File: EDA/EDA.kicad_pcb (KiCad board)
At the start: 2 copper layers, 75.4 x 53.8 mm, 46 parts, among them J2 Screw_Terminal_01x02, M1 Motor_Servo, U1 PMCF8316A1VRGFR, U2 LM2596S-5, U3 LM2678S-5

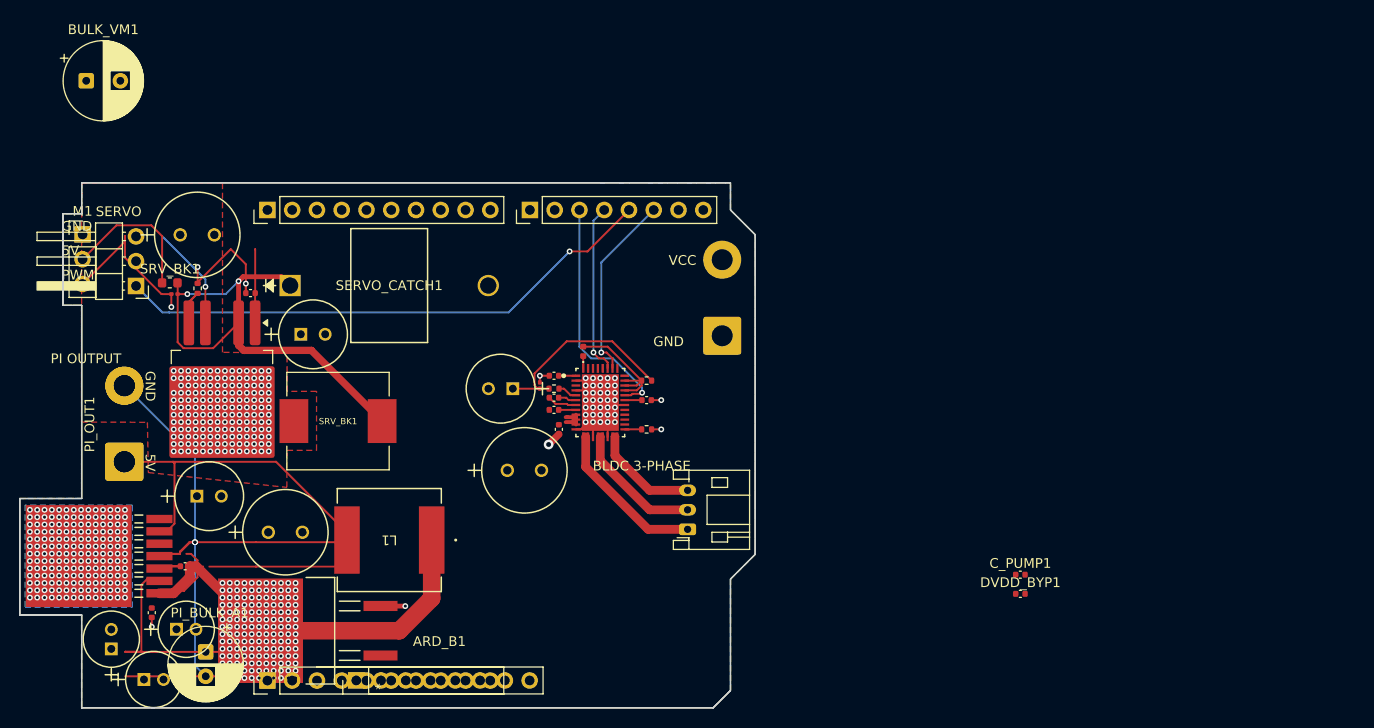
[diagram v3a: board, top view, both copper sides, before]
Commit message: Add initial EDA project files and configuration
- Created EDA.step file for project steps.
- Added autosave configuration for EDA.kicad_prl with board settings, visibility options, and net inspector panel configurations.
- Introduced lock files for PCB and schematic with hostname and username information.
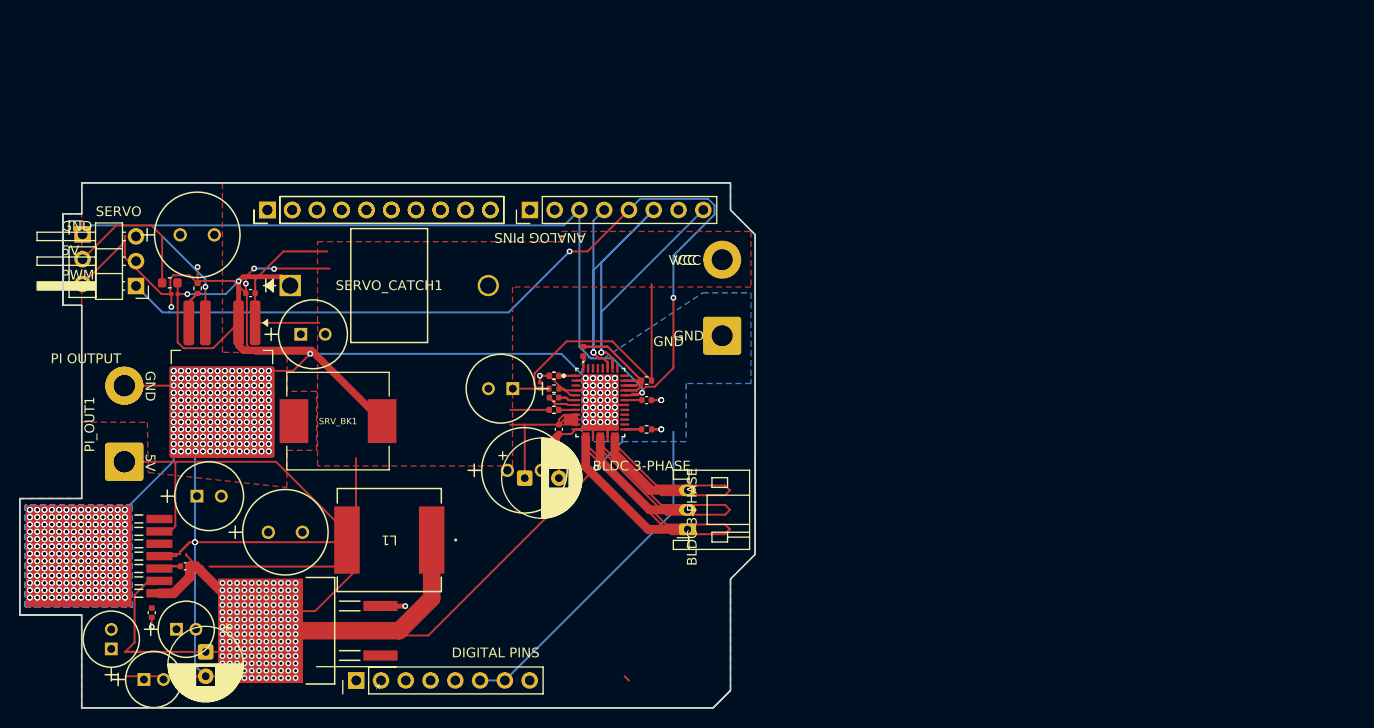
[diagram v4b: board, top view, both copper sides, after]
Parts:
- removed the ARD_B1 at (124.9, 73.8)
- removed the ARD_B1 at (124.9, 122.0)
- removed the C_PUMP1 at (154.2, 94.2)
- removed the C_PUMP1 at (202.1, 111.2)
- removed the DVDD_BYP1 at (154.2, 90.8)
- removed the DVDD_BYP1 at (202.1, 113.1)
- removed the PI_OUT1 at (110.2, 99.6) (x2)
- added ARD_B1 (x2): Conn_01x10_Pin, Connector_PinHeader_2.54mm:PinHeader_1x10_P2.54mm_Vertical, F.Cu at (124.9, 73.8)
- added C_PUMP1 (x2): 1uf, Capacitor_SMD:C_0402_1005Metric, F.Cu at (154.2, 94.2)
- added DVDD_BYP1 (x2): 1uf, Capacitor_SMD:C_0402_1005Metric, F.Cu at (154.2, 90.8)
- added PI_OUT1 (x2): Screw_Terminal_01x02, Connector_Wire:SolderWire-1.5sqmm_1x02_P7.8mm_D1.7mm_OD3.9mm, F.Cu at (110.2, 99.6)
- moved BULK_VM1 60.7 mm to (151.2, 101.2)
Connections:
- M1 pad 2: +5V -> SRV 5V, 3A
- SRV_BK1 pad 1: +5V -> SRV 5V, 3A
- U1 pad 5: Net-(U1-SW_BK) -> unconnected-(U1-SW_BK-Pad5)
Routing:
- net GND: track 123.7 -> 282.8 mm, vias 395 -> 786
- net 60: track 78.5 -> 0.00 mm, vias 1 -> 0
- net +7.5V: track 40.7 -> 103.0 mm
- net 63: track 0.00 -> 52.1 mm
- net SRV_PWM: track 56.0 -> 108.0 mm
- net SRV 5V, 3A: track 0.00 -> 39.0 mm
- net Net-(U2-~{ON}/OFF): track 3.40 -> 37.8 mm
- net Net-(ARD_C1-Pin_3): track 24.6 -> 58.7 mm, vias 1 -> 2
- net Net-(D_FAULT1-A): track 13.6 -> 43.3 mm
- net PI 5V, 5A: track 0.00 -> 25.6 mm, vias 0 -> 1
- net unconnected-(ARD_C1-Pin_8-Pad8): track 0.00 -> 21.4 mm, vias 0 -> 1
- net Net-(ARD_C1-Pin_6): track 19.3 -> 39.0 mm, vias 1 -> 2
- net unconnected-(ARD_B1-Pin_9-Pad9): track 13.7 -> 0.00 mm
- net Net-(U2-OUT): track 37.2 -> 50.8 mm
- net unconnected-(U1-FB_BK-Pad3): track 2.26 -> 13.6 mm
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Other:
- outline, holes or cut-outs redrawn
- board text added: "ANALOG PINS"
- board text added: "DIGITAL PINS"
- board text added: "SERVO OUT"

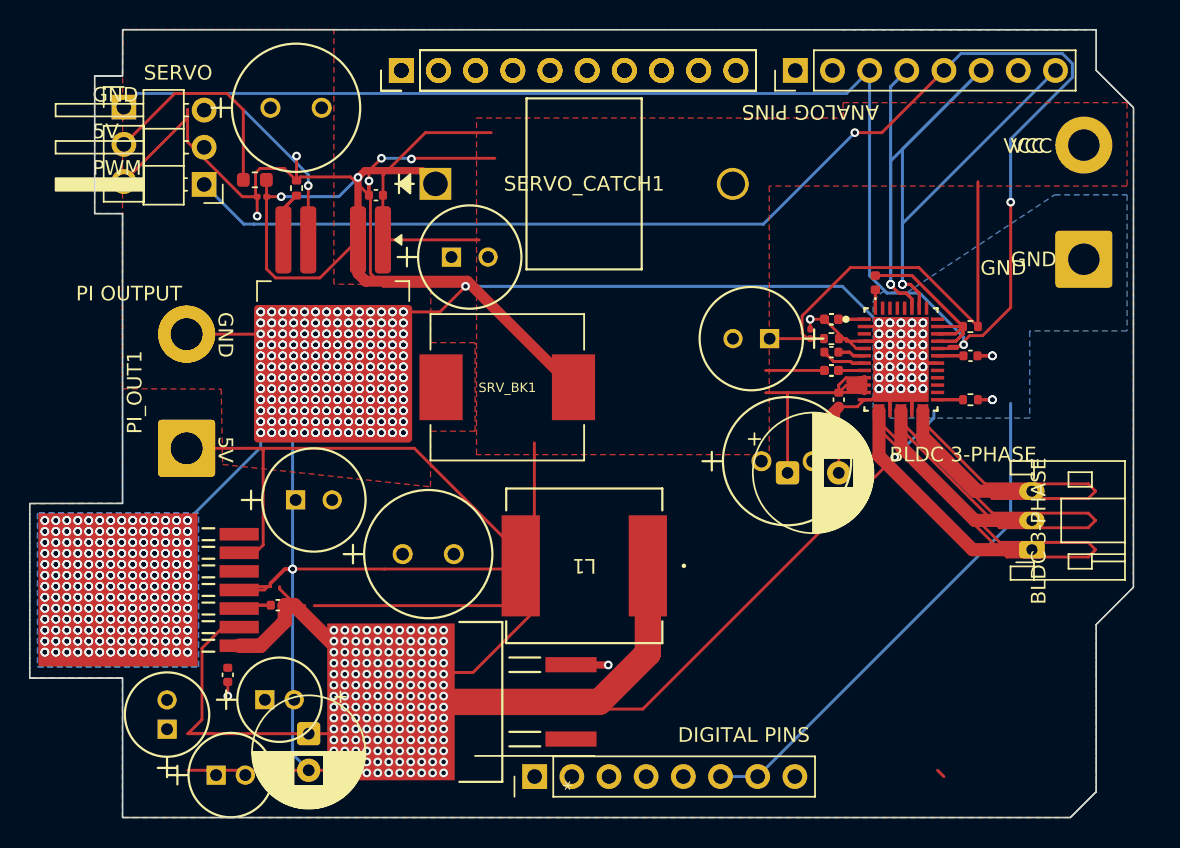
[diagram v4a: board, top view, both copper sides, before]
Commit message: Add new symbols and footprints for UCY2D181MHD3TN and VS-6TQ045S-M3 components
- Created symbol for UCY2D181MHD3TN with properties including reference, value, footprint, and datasheet.
- Added footprint for UCY2D181MHD3TN with dimensions and pad specifications.
- Created symbol for VS-6TQ045S-M3 with properties including reference, value, footprint, and datasheet link.
- Added multiple footprints for VS-6TQ045S-M3, including DPAK_045S-M3_VIS, DPAK_045S-M3_VIS-L, and DPAK_045S-M3_VIS-M with detailed specifications.
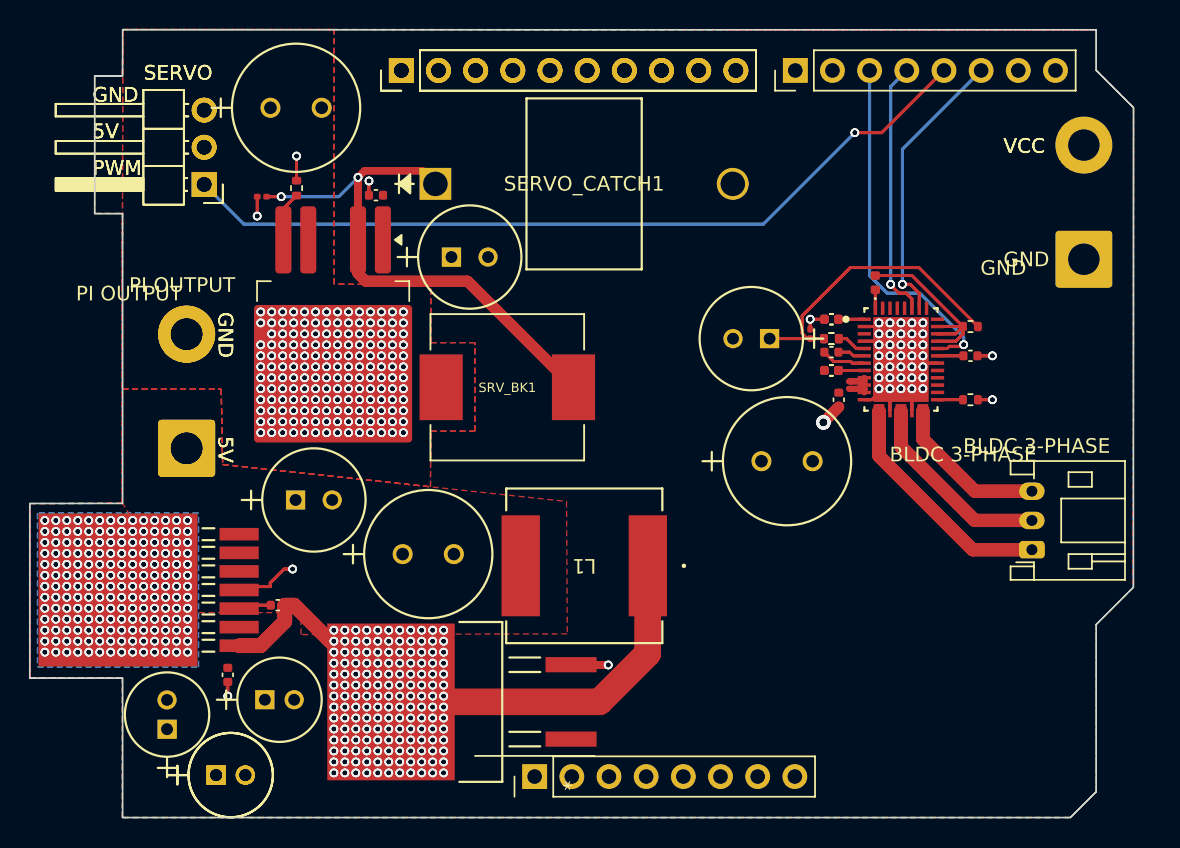
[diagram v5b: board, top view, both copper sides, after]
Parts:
- removed the ARD_B1 at (124.9, 73.8) (x2)
- removed BULK_VM1: 500uf, Capacitor_THT:CP_Radial_D8.0mm_P3.50mm
- removed the C_PUMP1 at (154.2, 94.2) (x2)
- removed the DVDD_BYP1 at (154.2, 90.8) (x2)
- removed the M1 at (111.4, 81.5)
- removed the M1 at (105.9, 76.3)
- removed the PI_BULK1 at (112.2, 121.9)
- removed PI_BULK_A1: 15uf, Capacitor_THT:CP_Radial_D7.5mm_P2.50mm
- removed the PI_OUT1 at (110.2, 99.6) (x2)
- removed the R_BK1 at (154.2, 92.1)
- removed the SRV_BK1 at (114.8, 81.2)
- added ARD_B1 (x2): Conn_01x10_Pin, Connector_PinHeader_2.54mm:PinHeader_1x10_P2.54mm_Vertical, F.Cu at (124.9, 73.8)
- added C_PUMP1 (x2): 1uf, Capacitor_SMD:C_0402_1005Metric, F.Cu at (154.2, 94.2)
- added DVDD_BYP1 (x2): 1uf, Capacitor_SMD:C_0402_1005Metric, F.Cu at (154.2, 90.8)
- added M1 (x2): Motor_Servo, Connector_PinHeader_2.54mm:PinHeader_1x03_P2.54mm_Horizontal, F.Cu at (111.4, 81.5)
- added PI_BULK1 (x2): 15uf, 860160572002:CAP_5X11_WRE, F.Cu at (112.2, 121.9)
- added PI_OUT1 (x2): Screw_Terminal_01x02, Connector_Wire:SolderWire-1.5sqmm_1x02_P7.8mm_D1.7mm_OD3.9mm, F.Cu at (110.2, 99.6)
- added R_BK1 (x2): 5.1k, Resistor_SMD:R_0402_1005Metric, F.Cu at (154.2, 92.1)
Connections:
- U1 pad 5: unconnected-(U1-SW_BK-Pad5) -> Net-(U1-SW_BK)
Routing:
- net GND: track 282.8 -> 52.6 mm, vias 786 -> 788
- net +7.5V: track 103.0 -> 6.20 mm
- net 63: track 52.1 -> 0.00 mm
- net Net-(U3-SW): track 39.8 -> 79.6 mm, vias 154 -> 308
- net SRV 5V, 3A: track 39.0 -> 0.00 mm
- net Net-(U2-~{ON}/OFF): track 37.8 -> 6.80 mm
- net PI 5V, 5A: track 25.6 -> 0.00 mm, vias 1 -> 0
- net Net-(U2-OUT): track 50.8 -> 74.3 mm, vias 2 -> 4
- net unconnected-(ARD_C1-Pin_8-Pad8): track 21.4 -> 0.00 mm, vias 1 -> 0
- net +3V3: track 21.9 -> 41.3 mm
- net Net-(ARD_C1-Pin_4): track 17.6 -> 35.2 mm, vias 1 -> 2
- net Net-(BLDC_3P1-Pin_1): track 16.7 -> 33.4 mm
- net Net-(D_FAULT1-A): track 43.3 -> 27.1 mm
- net Net-(BLDC_3P1-Pin_2): track 14.0 -> 28.0 mm
- net unconnected-(U1-FB_BK-Pad3): track 13.6 -> 0.00 mm
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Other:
- board text removed: "ANALOG PINS"
- board text removed: "DIGITAL PINS"
- board text removed: "SERVO OUT"
